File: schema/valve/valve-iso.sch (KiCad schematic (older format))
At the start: 10 parts, among them Q8 MOSFET_N, Q9 bc847, U8 PHDARL

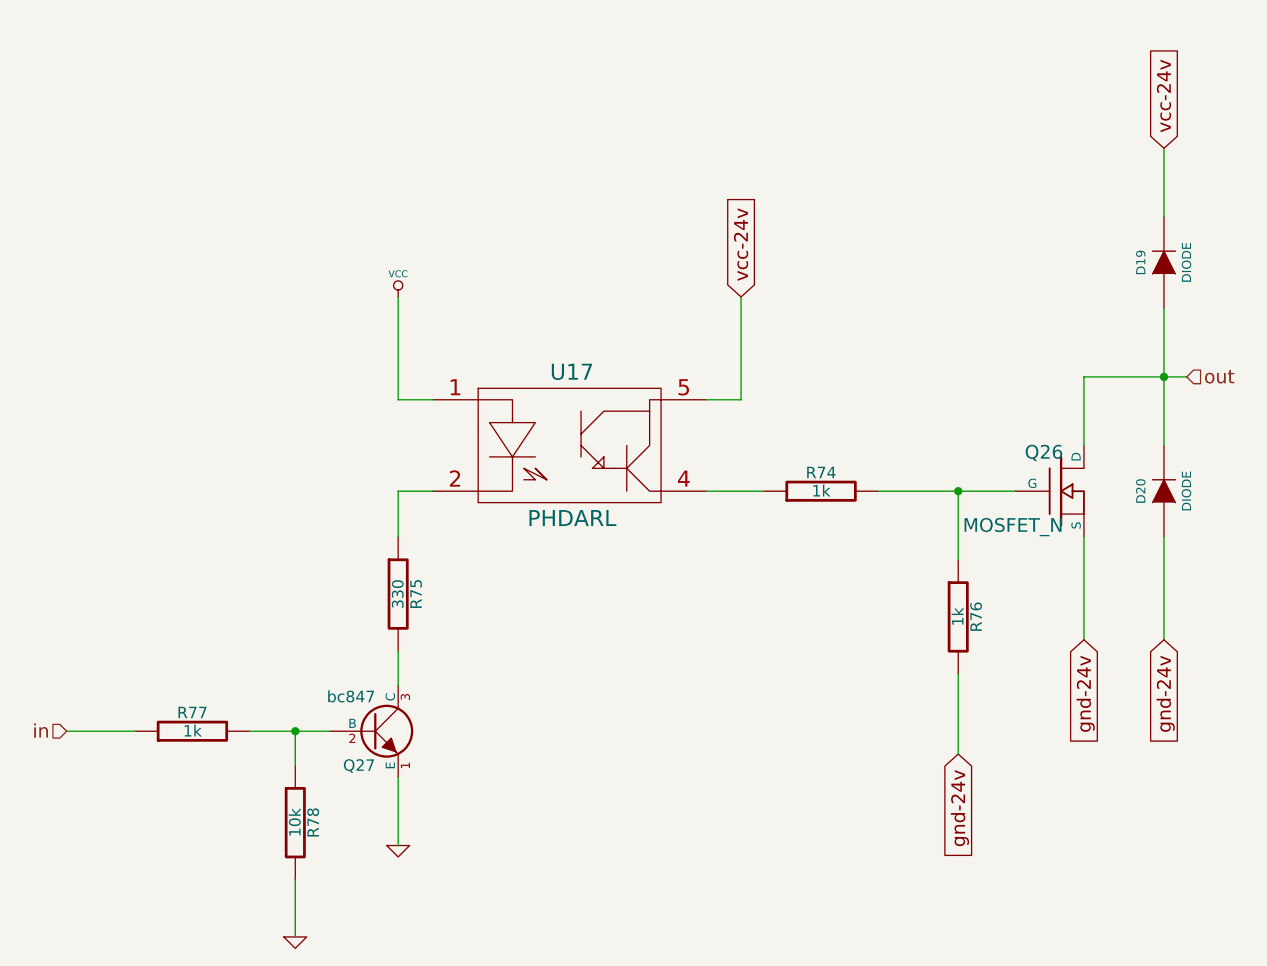
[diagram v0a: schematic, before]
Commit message: Added filtering capacitors.
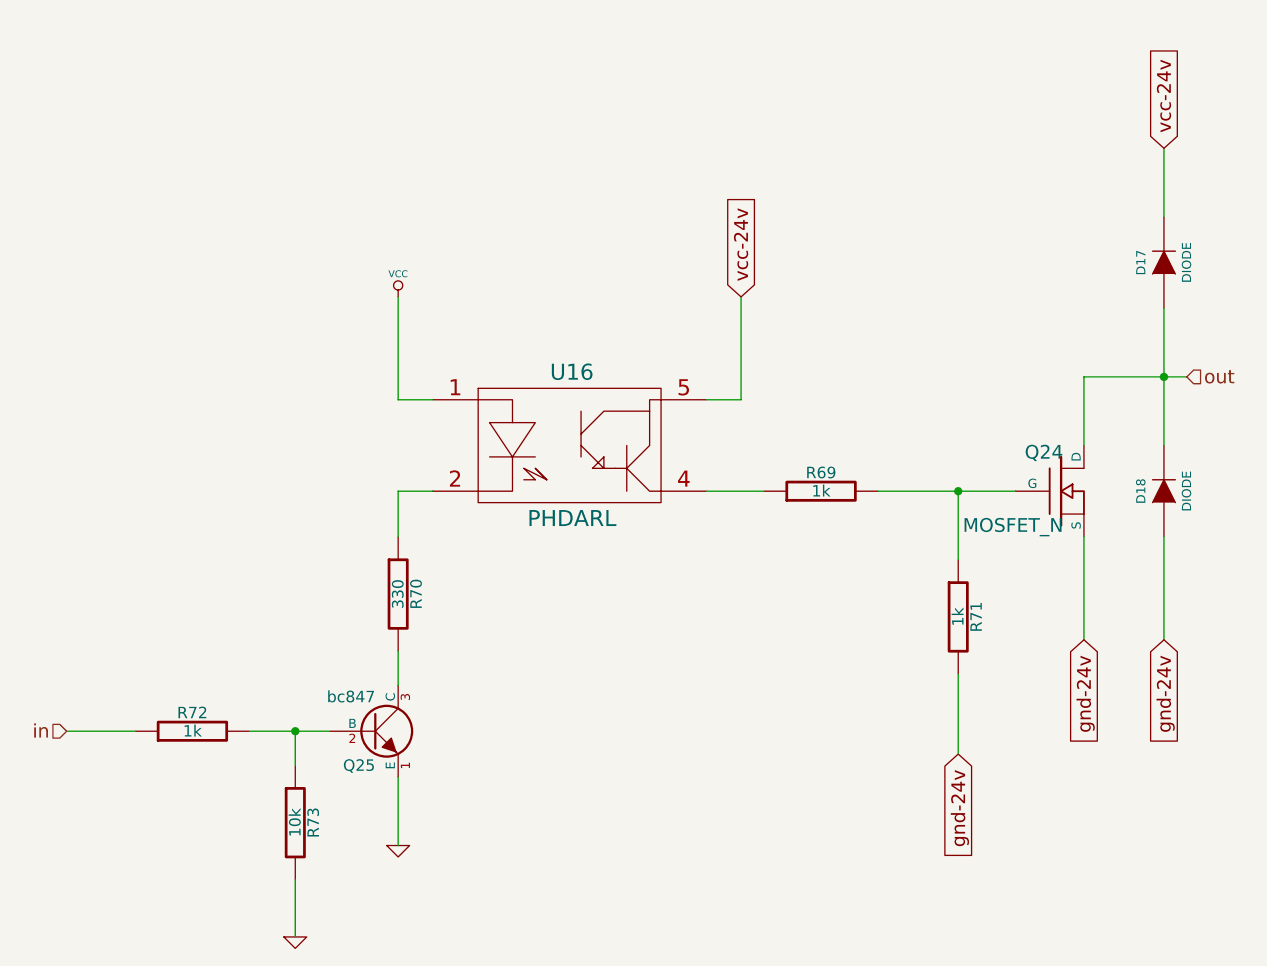
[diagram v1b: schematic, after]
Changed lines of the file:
@@
-EESchema Schematic File Version 2  date Tue 03 Apr 2012 12:20:51 AM MSK
+EESchema Schematic File Version 2  date Tue 03 Apr 2012 01:04:14 AM MSK
 LIBS:power
 LIBS:device
@@
 $Descr A4 11700 8267
 encoding utf-8
-Sheet 18 45
+Sheet 40 45
 Title ""
 Date "2 apr 2012"
@@
 AR Path="/4F79F54D/4F79EE31" Ref="D17"  Part="1"
 AR Path="/4F79E923/4F79EE31" Ref="D19"  Part="1"
-F 0 "D19" H 7800 3300 40  0000 C CNN
+F 0 "D17" H 7800 3300 40  0000 C CNN
 F 1 "DIODE" H 7800 3100 40  0000 C CNN
 	1    7800 3200
@@
 AR Path="/4F79F54D/4F79EE29" Ref="D18"  Part="1"
 AR Path="/4F79E923/4F79EE29" Ref="D20"  Part="1"
-F 0 "D20" H 7800 4300 40  0000 C CNN
+F 0 "D18" H 7800 4300 40  0000 C CNN
 F 1 "DIODE" H 7800 4100 40  0000 C CNN
 	1    7800 4200
@@
 AR Path="/4F79F54D/4F79ED4B" Ref="#PWR53"  Part="1"
 AR Path="/4F79E923/4F79ED4B" Ref="#PWR56"  Part="1"
-F 0 "#PWR56" H 4450 3450 30  0001 C CNN
+F 0 "#PWR53" H 4450 3450 30  0001 C CNN
 F 1 "VCC" H 4450 3450 30  0000 C CNN
 	1    4450 3350
@@
 AR Path="/4F79F54D/4F79EC92" Ref="R69"  Part="1"
 AR Path="/4F79E923/4F79EC92" Ref="R74"  Part="1"
-F 0 "R74" V 6380 4200 50  0000 C CNN
+F 0 "R69" V 6380 4200 50  0000 C CNN
 F 1 "1k" V 6300 4200 50  0000 C CNN
 	1    6300 4200
@@
 AR Path="/4F79F54D/4F79EC7E" Ref="R71"  Part="1"
 AR Path="/4F79E923/4F79EC7E" Ref="R76"  Part="1"
-F 0 "R76" V 6980 4750 50  0000 C CNN
+F 0 "R71" V 6980 4750 50  0000 C CNN
 F 1 "1k" V 6900 4750 50  0000 C CNN
 	1    6900 4750
@@
 AR Path="/4F79F54D/4F79EC1C" Ref="Q24"  Part="1"
 AR Path="/4F79E923/4F79EC1C" Ref="Q26"  Part="1"
-F 0 "Q26" H 7360 4370 60  0000 R CNN
+F 0 "Q24" H 7360 4370 60  0000 R CNN
 F 1 "MOSFET_N" H 7360 4050 60  0000 R CNN
 	1    7350 4200
@@
 AR Path="/4F79F54D/4F79EBE4" Ref="#PWR55"  Part="1"
 AR Path="/4F79E923/4F79EBE4" Ref="#PWR58"  Part="1"
-F 0 "#PWR58" H 4000 6150 30  0001 C CNN
+F 0 "#PWR55" H 4000 6150 30  0001 C CNN
 F 1 "GND" H 4000 6080 30  0001 C CNN
 	1    4000 6150
@@
 AR Path="/4F79F54D/4F79EBD8" Ref="R73"  Part="1"
 AR Path="/4F79E923/4F79EBD8" Ref="R78"  Part="1"
-F 0 "R78" V 4080 5650 50  0000 C CNN
+F 0 "R73" V 4080 5650 50  0000 C CNN
 F 1 "10k" V 4000 5650 50  0000 C CNN
 	1    4000 5650
@@
 AR Path="/4F79F54D/4F79EBD0" Ref="R72"  Part="1"
 AR Path="/4F79E923/4F79EBD0" Ref="R77"  Part="1"
-F 0 "R77" V 3630 5250 50  0000 C CNN
+F 0 "R72" V 3630 5250 50  0000 C CNN
 F 1 "1k" V 3550 5250 50  0000 C CNN
 	1    3550 5250
@@
 AR Path="/4F79F54D/4F79EBCA" Ref="#PWR54"  Part="1"
 AR Path="/4F79E923/4F79EBCA" Ref="#PWR57"  Part="1"
-F 0 "#PWR57" H 4450 5750 30  0001 C CNN
+F 0 "#PWR54" H 4450 5750 30  0001 C CNN
 F 1 "GND" H 4450 5680 30  0001 C CNN
 	1    4450 5750
@@
 AR Path="/4F79F54D/4F79EBB8" Ref="R70"  Part="1"
 AR Path="/4F79E923/4F79EBB8" Ref="R75"  Part="1"
-F 0 "R75" V 4530 4650 50  0000 C CNN
+F 0 "R70" V 4530 4650 50  0000 C CNN
 F 1 "330" V 4450 4650 50  0000 C CNN
 	1    4450 4650
@@
 AR Path="/4F79F54D/4F79EB99" Ref="Q25"  Part="1"
 AR Path="/4F79E923/4F79EB99" Ref="Q27"  Part="1"
-F 0 "Q27" H 4350 5100 50  0000 R CNN
+F 0 "Q25" H 4350 5100 50  0000 R CNN
 F 1 "bc847" H 4350 5400 50  0000 R CNN
 	1    4350 5250
@@
 AR Path="/4F79F54D/4F79EB8E" Ref="U16"  Part="1"
 AR Path="/4F79E923/4F79EB8E" Ref="U17"  Part="1"
-F 0 "U17" H 5210 4320 70  0000 C CNN
+F 0 "U16" H 5210 4320 70  0000 C CNN
 F 1 "PHDARL" H 5210 3680 70  0000 C CNN
 	1    5200 4000

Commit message: Schema, svg and png.
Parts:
- renumbered Q9 to Q16, Q8 to Q17, R32 to R61, R33 to R62, R30 to R63, R29 to R64, R31 to R65, U8 to U16
